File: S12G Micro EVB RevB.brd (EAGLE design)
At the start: 49 x 21 mm, 42 parts, among them IC1 FT232RL, IC2 MCP1640, J2 JUMPER, J3 JUMPER

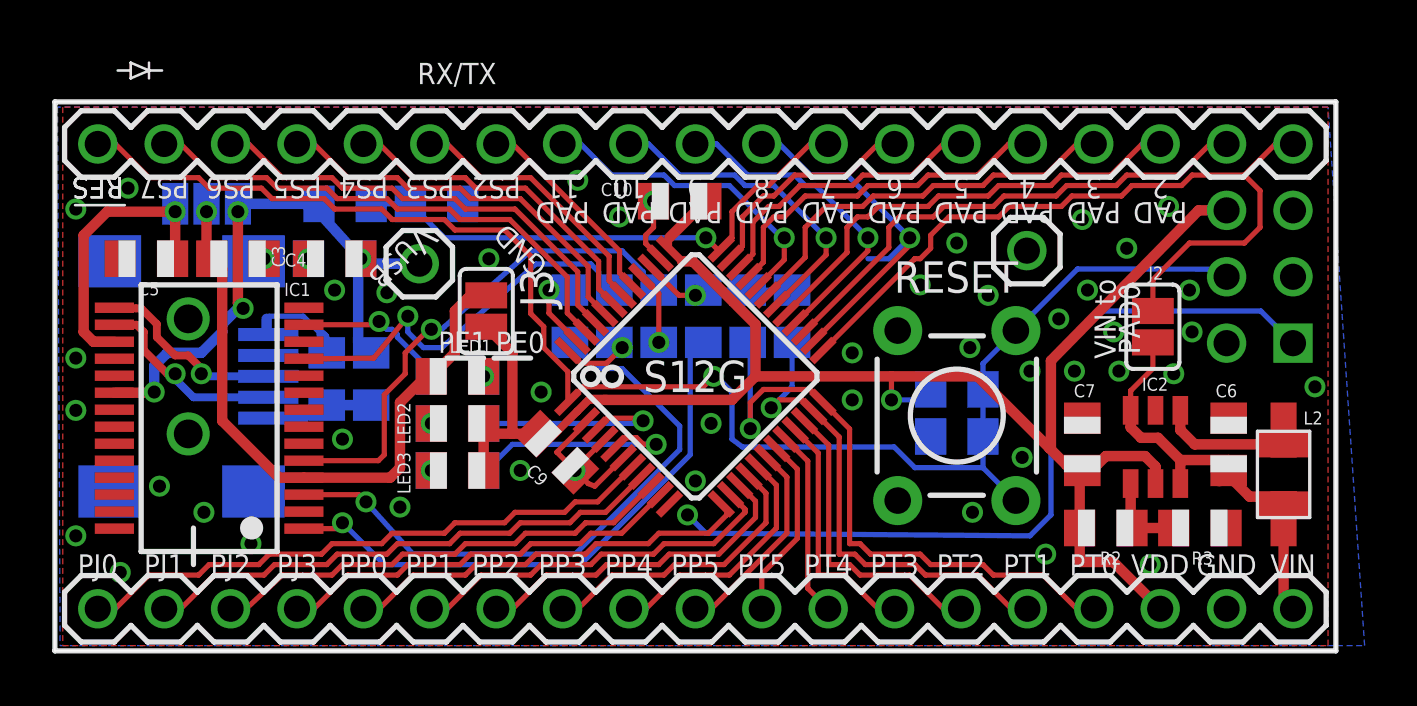
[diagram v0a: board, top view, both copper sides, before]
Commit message: finished RevB layout
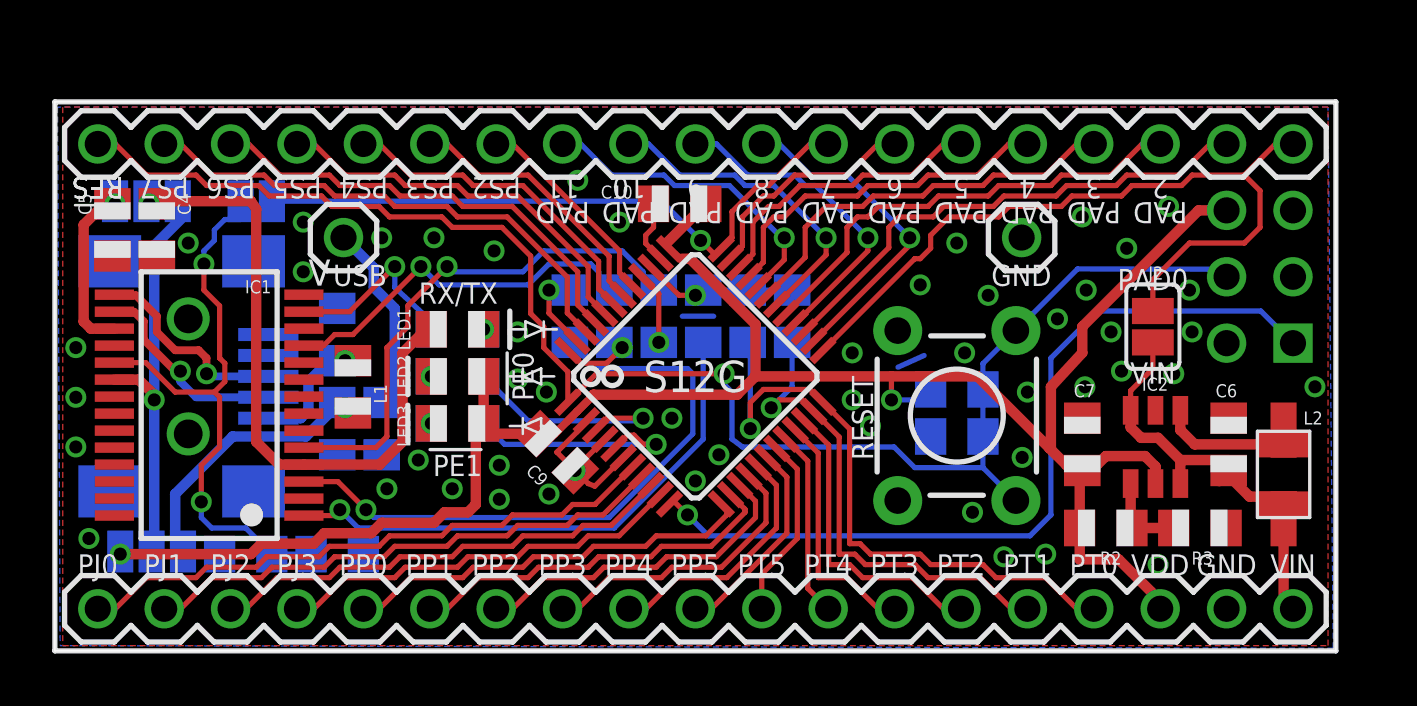
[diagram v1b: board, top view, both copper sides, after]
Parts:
- added J4: (no value), myLibrary:JUMPER_2WAY
- R10, R11, R12, R9: value 2K2 -> 100
- R14: value 10K -> 4.7K
- moved R13 13.9 mm to (11.3, 5.70)
- moved R14 13.9 mm to (7.80, 5.70)
- moved J3 9.75 mm to (8.20, 19.2), flipped to the bottom, turned to 0 degrees
- moved C2 6.74 mm to (13.0, 10.5), turned to 270 degrees
- moved C3 6.50 mm to (11.3, 10.5), flipped to the bottom, turned to 270 degrees
- moved C4 3.29 mm to (4.40, 18.1), turned to 90 degrees
- moved VUSB 3.07 mm to (11.5, 17.8)
- moved J1 2.30 mm to (4.00, 19.2)
- moved LED1 1.80 mm to (15.9, 14.3)
- moved LED2 1.80 mm to (15.9, 12.5)
- moved R1 1.80 mm to (15.9, 14.3)
- moved R7 1.80 mm to (15.9, 12.5)
- moved LED3 1.80 mm to (15.9, 10.7)
- moved R8 1.80 mm to (15.9, 10.7)
- moved C1 1.75 mm to (11.3, 14.1)
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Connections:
- net VIN renamed V+
- new net N$4: IC1.19, J3.2, R13.1, R14.2
- new net VCC: IC1.20, J1.1, J4.2
- net PAD7: now also J3.1; no longer R13.1, R14.2
- net VCCIO: no longer J3.1
- net VDD: now also J4.1; no longer J3.2
- net VDDUSB: now also J4.3; no longer IC1.20, J1.1
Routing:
- net N$4: track 0.00 -> 23.0 mm, vias 0 -> 2
- net VCC: track 0.00 -> 15.9 mm, vias 0 -> 1
- net VDD: track 67.3 -> 80.5 mm, vias 1 -> 2
- net 3V3OUT: track 11.0 -> 6.22 mm
- net PAD7: track 20.5 -> 24.4 mm
- net CBUS2: track 5.93 -> 7.92 mm
- net PAD8: track 14.6 -> 12.6 mm
- net GND: track 13.2 -> 11.6 mm, vias 47 -> 50
- net BKGD: track 31.1 -> 32.0 mm
- net TXD_FT232RL: track 21.9 -> 20.9 mm
- net CTS_FT232RL: track 15.2 -> 14.3 mm
- net N$5: track 0.93 -> 0.00 mm
- net RTS_FT232RL: track 23.5 -> 24.3 mm
- net VCCIO: track 24.9 -> 24.2 mm
- net RXD_FT232RL: track 19.3 -> 20.0 mm
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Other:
- board text added: "3.3V"
- board text added: "PAD7"
- board text added: "RevB"
- board text added: "S12G-Micro-EVB"
- board text added: "VDDUSB"
- board text removed: "3V3"
- board text removed: "Rev. A"
- board text removed: "S12G Micro EVB"
- board text removed: "VIN to"
